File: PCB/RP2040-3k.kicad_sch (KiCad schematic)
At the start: 46 parts, among them J1 USB_C_Receptacle_USB2.0, J2 Conn_01x06, SW1 MX_SW_HS, SW2 MX_SW_HS, SW3 MX_SW_HS, U1 RP2040, U2 SRV05-4, U3 XC6206PxxxMR, U4 W25Q16JVUXIQ, Y1 Crystal_GND24_Small

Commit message: Finished routing PCB
W25Q16JVUXIQTR library removed. Not using that part. Dimension changes made and other schematic things.
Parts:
- removed J2: Conn_01x06, symbol Connector_Generic:Conn_01x06
- added J2: Conn_01x02, Connector_PinHeader_2.54mm:PinHeader_1x02_P2.54mm_Vertical, symbol Connector_Generic:Conn_01x02
- U4: value W25Q16JVUXIQ -> W25Q32JVSS; footprint W25Q16JVUXIQTR part:PSON50P300X200X60-9N -> Package_SO:SOIC-8_5.23x5.23mm_P1.27mm
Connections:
- net COL0: now also U1.41 (GPIO29_ADC3)
- net COL1: now also U1.40 (GPIO28_ADC2)
- net COL2: now also U1.39 (GPIO27_ADC1)
- net GND: now also J2.1 (Pin_1)
- net SWITCHLED: now also U1.38 (GPIO26_ADC0)
- net UNDERGLOW: now also U1.37 (GPIO25)
- net at D1.2 (DOUT): now also D2.4 (DIN)
- net USB_BOOT renamed ~{USB_BOOT}
- net ~{USB_BOOT}: now also J2.2 (Pin_2)
- no-connect marks 4 -> 5
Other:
- note added: "REMOVED"

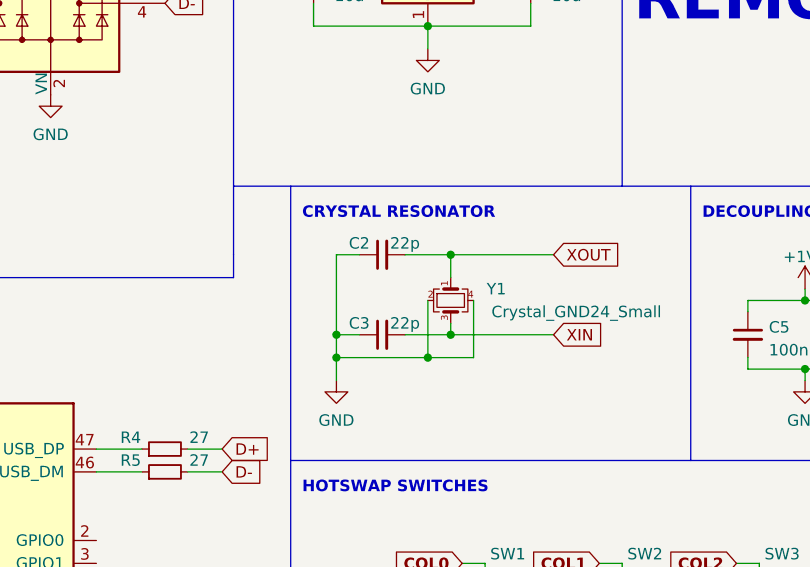
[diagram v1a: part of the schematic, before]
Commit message: Redid traces to tolerance
Clearance is now 0.2mm across the board. I also generated gerber files and etc
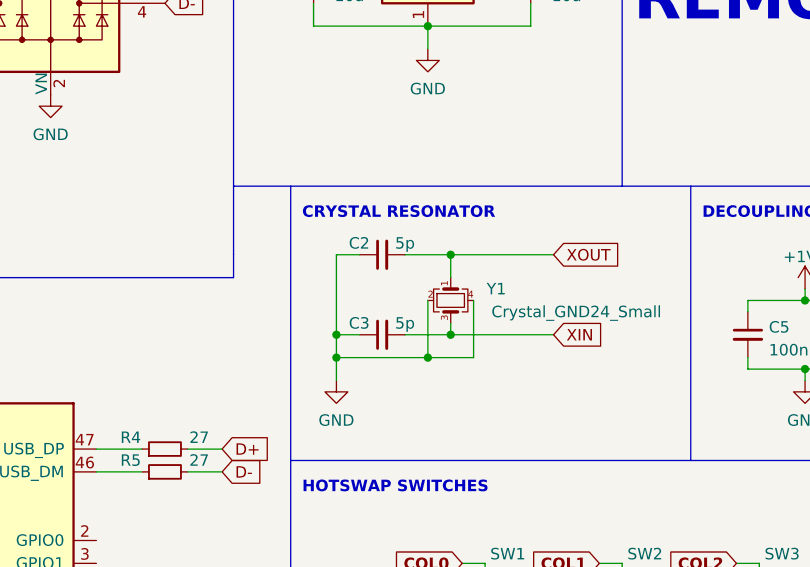
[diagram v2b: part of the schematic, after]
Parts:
- C2, C3: value 22p -> 5p
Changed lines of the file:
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@@
     (in_bom yes) (on_board yes)
     (property "Reference" "C2" (id 0) (at 128.27 68.58 90))
-    (property "Value" "22p" (id 1) (at 133.35 68.58 90))
+    (property "Value" "5p" (id 1) (at 133.35 68.58 90))
     (property "Footprint" "Capacitor_SMD:C_0402_1005Metric" (id 2) (at 130.81 69.85 0)
       (effects (font (size 1.27 1.27)) hide)
@@
     (in_bom yes) (on_board yes)
     (property "Reference" "C3" (id 0) (at 128.27 77.47 90))
-    (property "Value" "22p" (id 1) (at 133.35 77.47 90))
+    (property "Value" "5p" (id 1) (at 133.35 77.47 90))
     (property "Footprint" "Capacitor_SMD:C_0402_1005Metric" (id 2) (at 130.81 78.74 0)
       (effects (font (size 1.27 1.27)) hide)
@@
     )
     (path "/286ddfa6-090e-4c89-8a84-b51b9b4f2a98"
-      (reference "C2") (unit 1) (value "22p") (footprint "Capacitor_SMD:C_0402_1005Metric")
+      (reference "C2") (unit 1) (value "5p") (footprint "Capacitor_SMD:C_0402_1005Metric")
     )
     (path "/73467419-f6d1-498f-b04e-fa44356aac02"
-      (reference "C3") (unit 1) (value "22p") (footprint "Capacitor_SMD:C_0402_1005Metric")
+      (reference "C3") (unit 1) (value "5p") (footprint "Capacitor_SMD:C_0402_1005Metric")
     )
     (path "/fd8fae10-9e3e-4c5e-b5d1-775edfaccc0f"

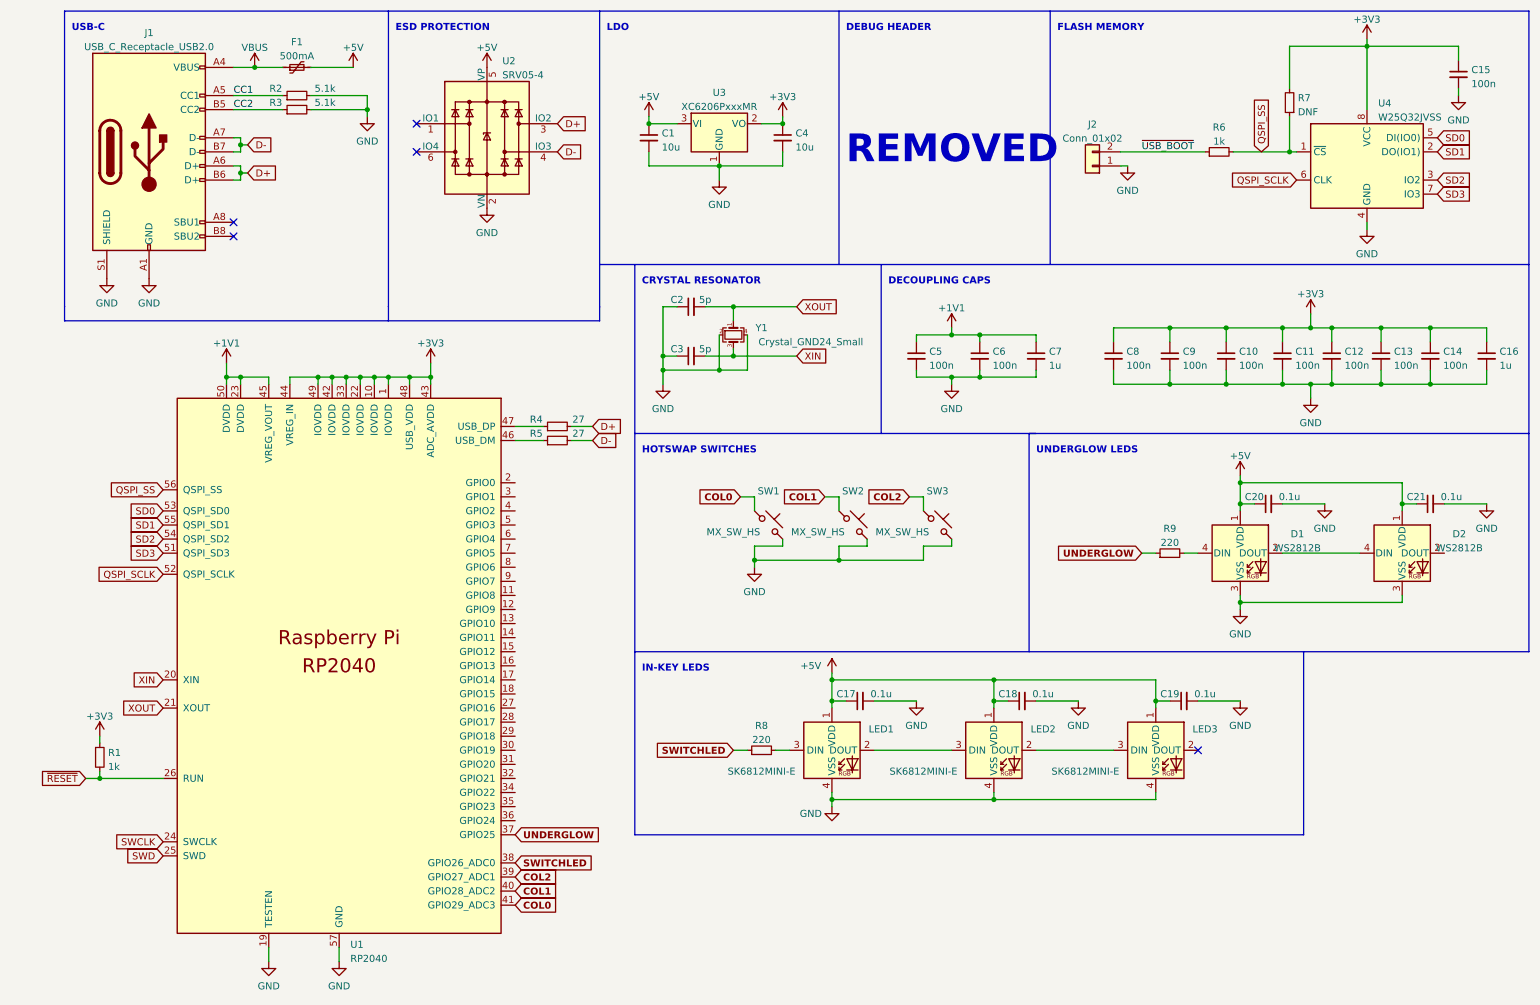
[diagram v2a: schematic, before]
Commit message: Fixed values and redid traces
Changed the data traces to be thicker. Redid crystal capacitor values (I originally calculated them wrongly). Changed 0.1uF values to 100nF for consistency. Regenerated BOM with updated changes
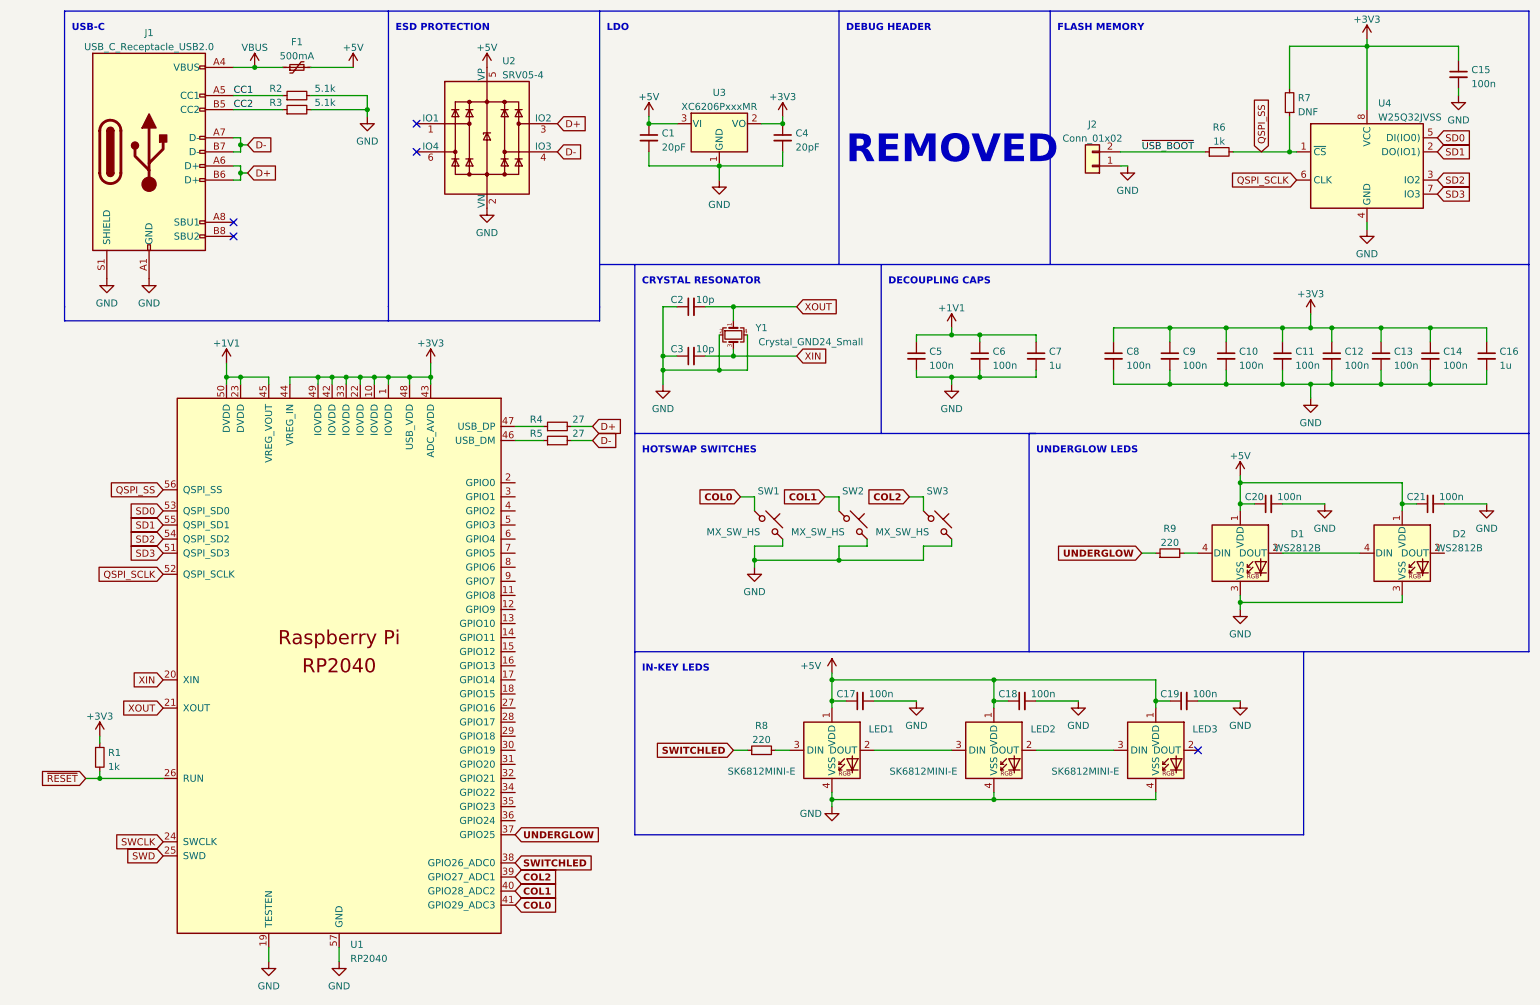
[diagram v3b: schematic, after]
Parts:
- C1, C4: value 10u -> 20pF
- C17, C18, C19, C20, C21: value 0.1u -> 100n
- C2, C3: value 5p -> 10p
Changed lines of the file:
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@@
     (in_bom yes) (on_board yes)
     (property "Reference" "C2" (id 0) (at 128.27 68.58 90))
-    (property "Value" "5p" (id 1) (at 133.35 68.58 90))
+    (property "Value" "10p" (id 1) (at 133.35 68.58 90))
     (property "Footprint" "Capacitor_SMD:C_0402_1005Metric" (id 2) (at 130.81 69.85 0)
       (effects (font (size 1.27 1.27)) hide)
@@
       (effects (font (size 1.27 1.27)) (justify left))
     )
-    (property "Value" "10u" (id 1) (at 125.5141 41.0785 0)
+    (property "Value" "20pF" (id 1) (at 125.5141 41.0785 0)
       (effects (font (size 1.27 1.27)) (justify left))
     )
@@
     (in_bom yes) (on_board yes)
     (property "Reference" "C3" (id 0) (at 128.27 77.47 90))
-    (property "Value" "5p" (id 1) (at 133.35 77.47 90))
+    (property "Value" "10p" (id 1) (at 133.35 77.47 90))
     (property "Footprint" "Capacitor_SMD:C_0402_1005Metric" (id 2) (at 130.81 78.74 0)
       (effects (font (size 1.27 1.27)) hide)
@@
     (in_bom yes) (on_board yes)
     (property "Reference" "C20" (id 0) (at 232.41 104.14 90))
-    (property "Value" "0.1u" (id 1) (at 238.76 104.14 90))
+    (property "Value" "100n" (id 1) (at 238.76 104.14 90))
     (property "Footprint" "Capacitor_SMD:C_0402_1005Metric" (id 2) (at 234.95 105.41 0)
       (effects (font (size 1.27 1.27)) hide)
@@
     (in_bom yes) (on_board yes)
     (property "Reference" "C17" (id 0) (at 158.75 139.7 90))
-    (property "Value" "0.1u" (id 1) (at 165.1 139.7 90))
+    (property "Value" "100n" (id 1) (at 165.1 139.7 90))
     (property "Footprint" "Capacitor_SMD:C_0402_1005Metric" (id 2) (at 161.29 140.97 0)
       (effects (font (size 1.27 1.27)) hide)
@@
     (in_bom yes) (on_board yes)
     (property "Reference" "C19" (id 0) (at 217.17 139.7 90))
-    (property "Value" "0.1u" (id 1) (at 223.52 139.7 90))
+    (property "Value" "100n" (id 1) (at 223.52 139.7 90))
     (property "Footprint" "Capacitor_SMD:C_0402_1005Metric" (id 2) (at 219.71 140.97 0)
       (effects (font (size 1.27 1.27)) hide)
@@
     (in_bom yes) (on_board yes)
     (property "Reference" "C18" (id 0) (at 187.96 139.7 90))
-    (property "Value" "0.1u" (id 1) (at 194.31 139.7 90))
+    (property "Value" "100n" (id 1) (at 194.31 139.7 90))
     (property "Footprint" "Capacitor_SMD:C_0402_1005Metric" (id 2) (at 190.5 140.97 0)
       (effects (font (size 1.27 1.27)) hide)
@@
     (in_bom yes) (on_board yes)
     (property "Reference" "C21" (id 0) (at 261.62 104.14 90))
-    (property "Value" "0.1u" (id 1) (at 267.97 104.14 90))
+    (property "Value" "100n" (id 1) (at 267.97 104.14 90))
     (property "Footprint" "Capacitor_SMD:C_0402_1005Metric" (id 2) (at 264.16 105.41 0)
       (effects (font (size 1.27 1.27)) hide)
@@
   )
   (symbol (lib_id "Device:C_Small") (at 147.32 39.37 0) (unit 1)
-    (in_bom yes) (on_board yes) (fields_autoplaced)
+    (in_bom yes) (on_board yes)
     (property "Reference" "C4" (id 0) (at 149.6441 38.5416 0)
       (effects (font (size 1.27 1.27)) (justify left))
     )
-    (property "Value" "10u" (id 1) (at 149.6441 41.0785 0)
+    (property "Value" "20pF" (id 1) (at 149.6441 41.0785 0)
       (effects (font (size 1.27 1.27)) (justify left))
     )
@@
     )
     (path "/3b517596-d7b3-4e54-85b4-0aa63c61a7e1"
-      (reference "C1") (unit 1) (value "10u") (footprint "Capacitor_SMD:C_0402_1005Metric")
+      (reference "C1") (unit 1) (value "20pF") (footprint "Capacitor_SMD:C_0402_1005Metric")
     )
     (path "/286ddfa6-090e-4c89-8a84-b51b9b4f2a98"
-      (reference "C2") (unit 1) (value "5p") (footprint "Capacitor_SMD:C_0402_1005Metric")
+      (reference "C2") (unit 1) (value "10p") (footprint "Capacitor_SMD:C_0402_1005Metric")
     )
     (path "/73467419-f6d1-498f-b04e-fa44356aac02"
-      (reference "C3") (unit 1) (value "5p") (footprint "Capacitor_SMD:C_0402_1005Metric")
+      (reference "C3") (unit 1) (value "10p") (footprint "Capacitor_SMD:C_0402_1005Metric")
     )
     (path "/fd8fae10-9e3e-4c5e-b5d1-775edfaccc0f"
-      (reference "C4") (unit 1) (value "10u") (footprint "Capacitor_SMD:C_0402_1005Metric")
+      (reference "C4") (unit 1) (value "20pF") (footprint "Capacitor_SMD:C_0402_1005Metric")
     )
     (path "/bc8559e9-dce1-4aac-9e8d-1c0cb05a4535"
@@
     )
     (path "/898514c3-d6b5-496f-9c28-f899924f4b94"
-      (reference "C17") (unit 1) (value "0.1u") (footprint "Capacitor_SMD:C_0402_1005Metric")
+      (reference "C17") (unit 1) (value "100n") (footprint "Capacitor_SMD:C_0402_1005Metric")
     )
     (path "/d7107086-2cf1-40a4-ae9e-8d911f3ab249"
-      (reference "C18") (unit 1) (value "0.1u") (footprint "Capacitor_SMD:C_0402_1005Metric")
+      (reference "C18") (unit 1) (value "100n") (footprint "Capacitor_SMD:C_0402_1005Metric")
     )
     (path "/c6a78658-aa0b-4410-b91b-19a7cc52acec"
-      (reference "C19") (unit 1) (value "0.1u") (footprint "Capacitor_SMD:C_0402_1005Metric")
+      (reference "C19") (unit 1) (value "100n") (footprint "Capacitor_SMD:C_0402_1005Metric")
     )
     (path "/800b1ec5-7265-4d26-b019-82ba68b397ea"
-      (reference "C20") (unit 1) (value "0.1u") (footprint "Capacitor_SMD:C_0402_1005Metric")
+      (reference "C20") (unit 1) (value "100n") (footprint "Capacitor_SMD:C_0402_1005Metric")
     )
     (path "/f4b16058-6956-4639-8a91-7d7a8c4d6252"
-      (reference "C21") (unit 1) (value "0.1u") (footprint "Capacitor_SMD:C_0402_1005Metric")
+      (reference "C21") (unit 1) (value "100n") (footprint "Capacitor_SMD:C_0402_1005Metric")
     )
     (path "/bbd4a14e-ef19-404a-9107-6873d915608a"

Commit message: Removed step up and fixed capacitor values
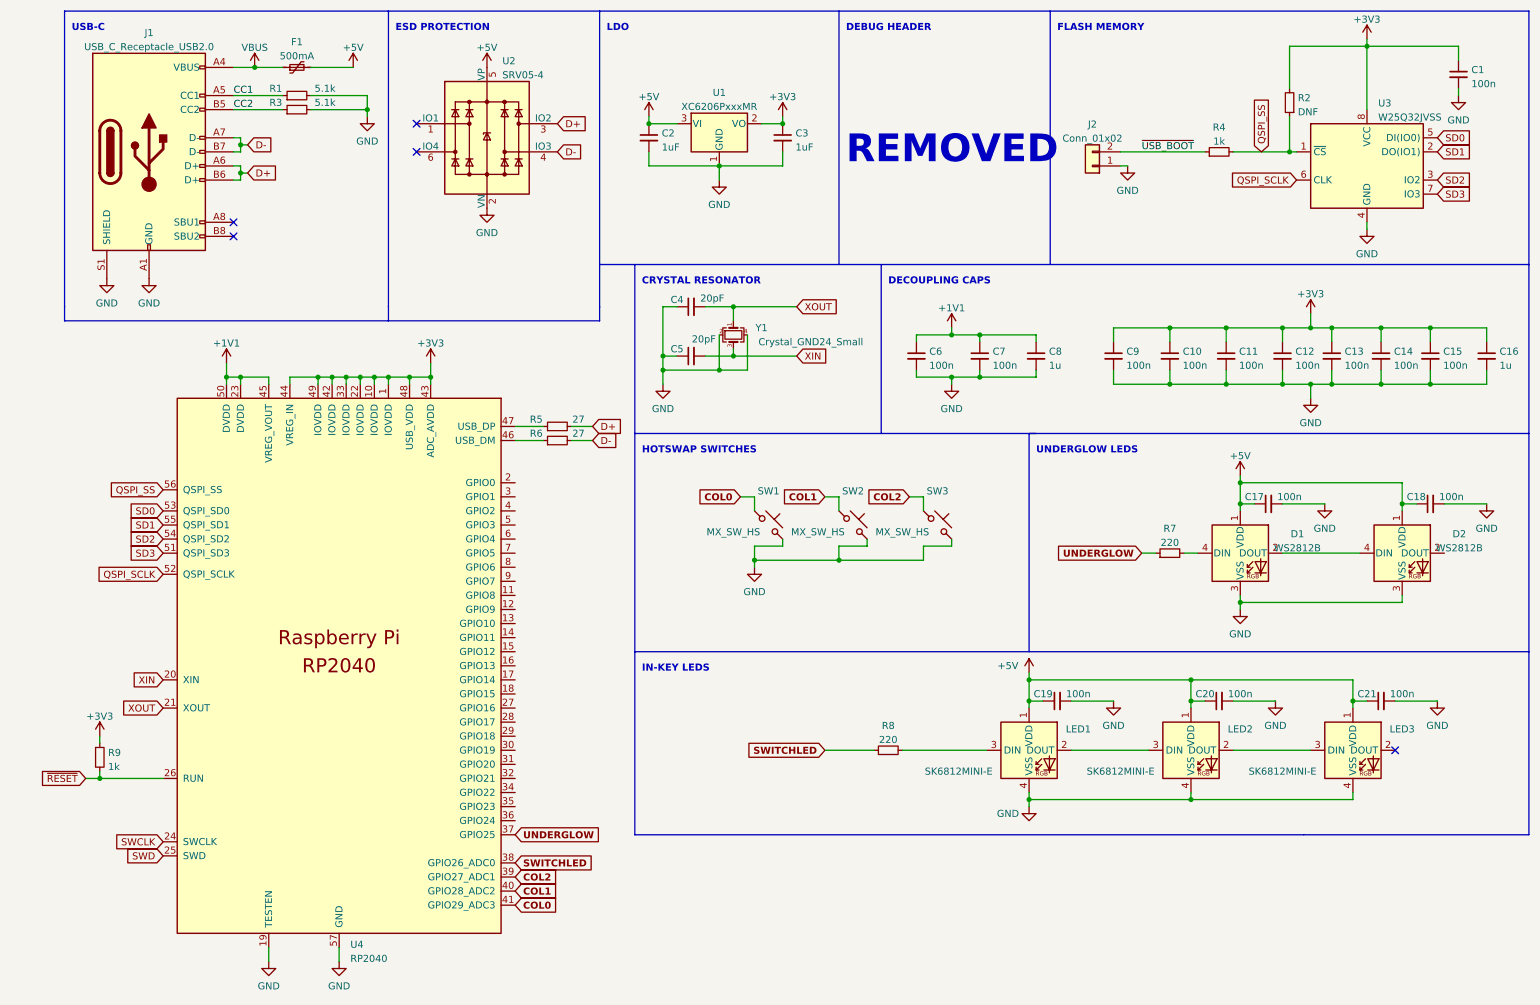
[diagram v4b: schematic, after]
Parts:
- C2: renamed from C1; value 20pF -> 1uF
- C3: renamed from C4; value 20pF -> 1uF
- C4: renamed from C2; value 10p -> 20pF
- C5: renamed from C3; value 10p -> 20pF
- renumbered C15 to C1, C9 to C10, C10 to C11, C11 to C12, C12 to C13, C13 to C14, C14 to C15, C20 to C17, C21 to C18, C17 to C19, C18 to C20, C19 to C21, C5 to C6, C6 to C7, C7 to C8, C8 to C9, R2 to R1, R7 to R2, R6 to R4, R4 to R5, R5 to R6, R9 to R7, R1 to R9, U3 to U1, U4 to U3, U1 to U4
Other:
- moved on the sheet: C19, C20, C21, LED1, LED2, LED3
